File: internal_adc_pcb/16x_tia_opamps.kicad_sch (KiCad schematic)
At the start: 46 parts, among them U14 TLV9064, U15 TLV9064, U16 TLV9064, U17 TLV9064

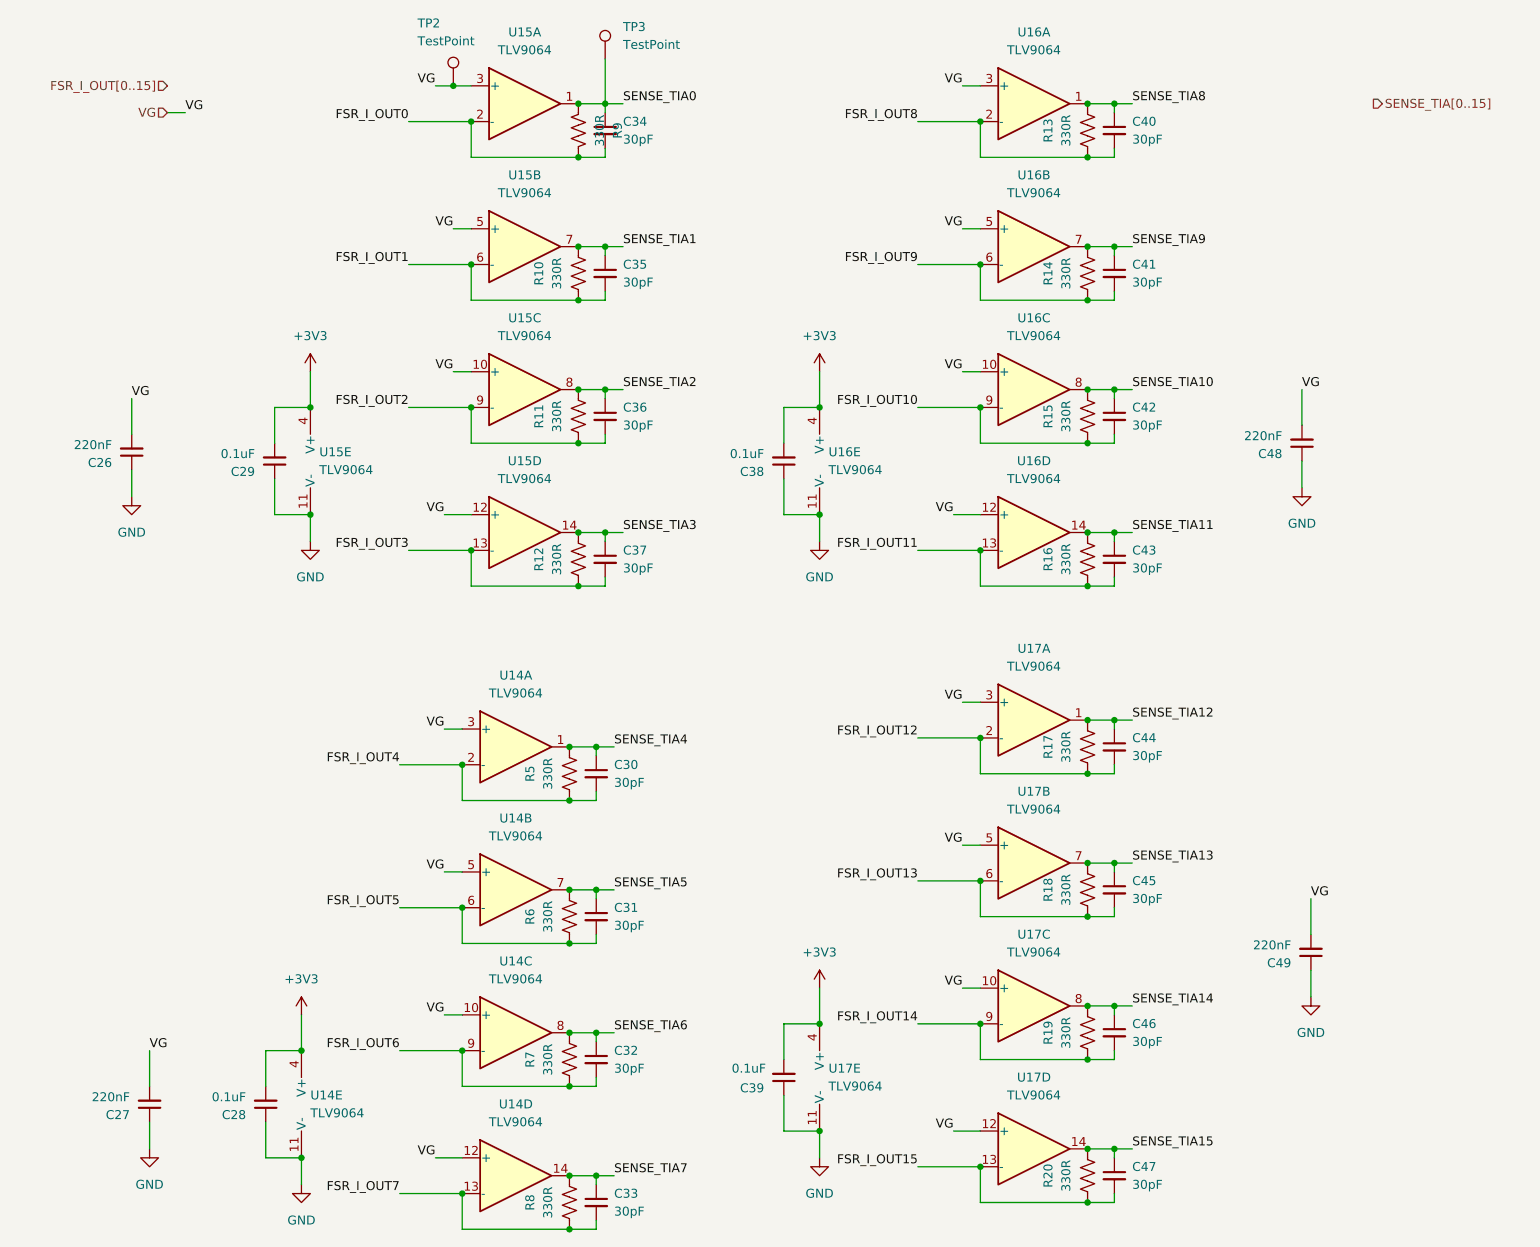
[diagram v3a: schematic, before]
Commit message: fixing all ERC errors for internal ADC ver, fixing warnings now
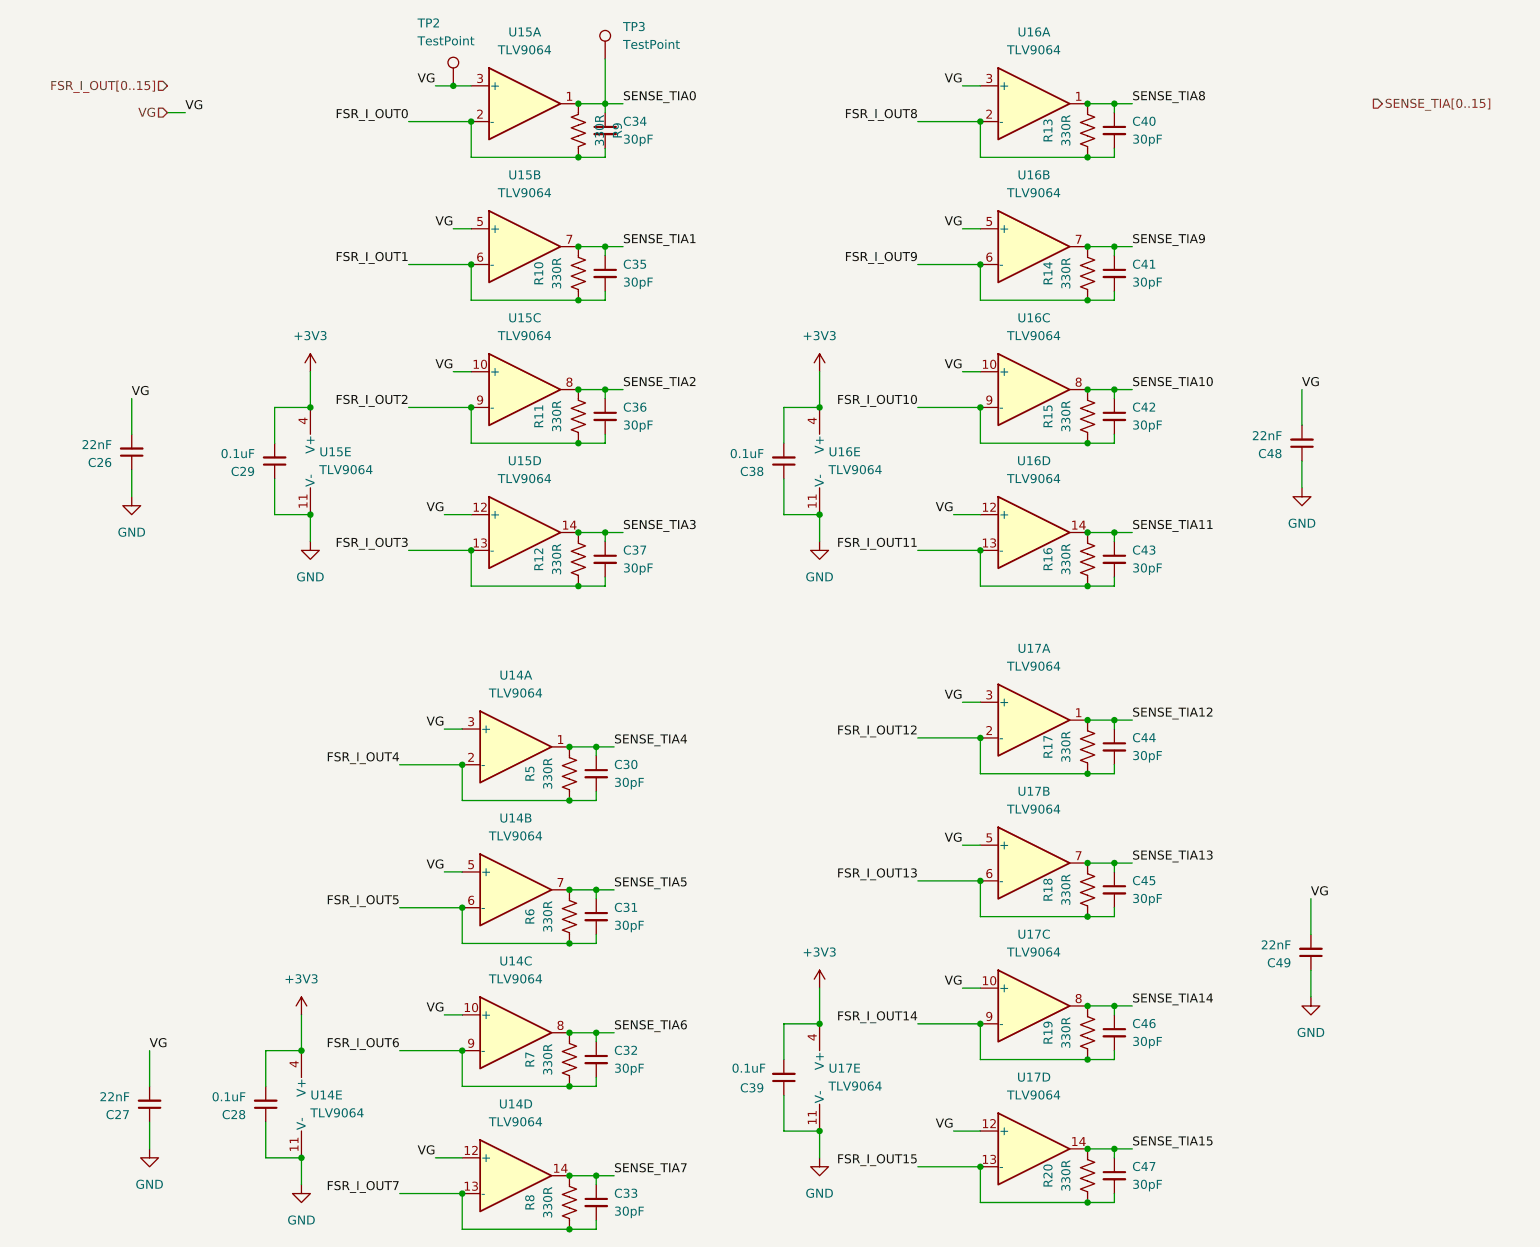
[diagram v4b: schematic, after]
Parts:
- C26, C27, C48, C49: value 220nF -> 22nF
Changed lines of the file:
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@@
 			)
 		)
-		(property "Value" "220nF"
+		(property "Value" "22nF"
 			(at 27.686 80.264 0)
 			(show_name no)
@@
 			)
 		)
-		(property "Value" "220nF"
+		(property "Value" "22nF"
 			(at 30.226 172.974 0)
 			(show_name no)
@@
 			)
 		)
-		(property "Value" "220nF"
+		(property "Value" "22nF"
 			(at 195.326 151.384 0)
 			(show_name no)
@@
 			)
 		)
-		(property "Value" "220nF"
+		(property "Value" "22nF"
 			(at 194.056 78.994 0)
 			(show_name no)
